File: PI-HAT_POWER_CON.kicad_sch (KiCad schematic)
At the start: 2 parts, among them J101 282834-2, J102 Raspberry_Pi_2x20_PTH_NoSilk

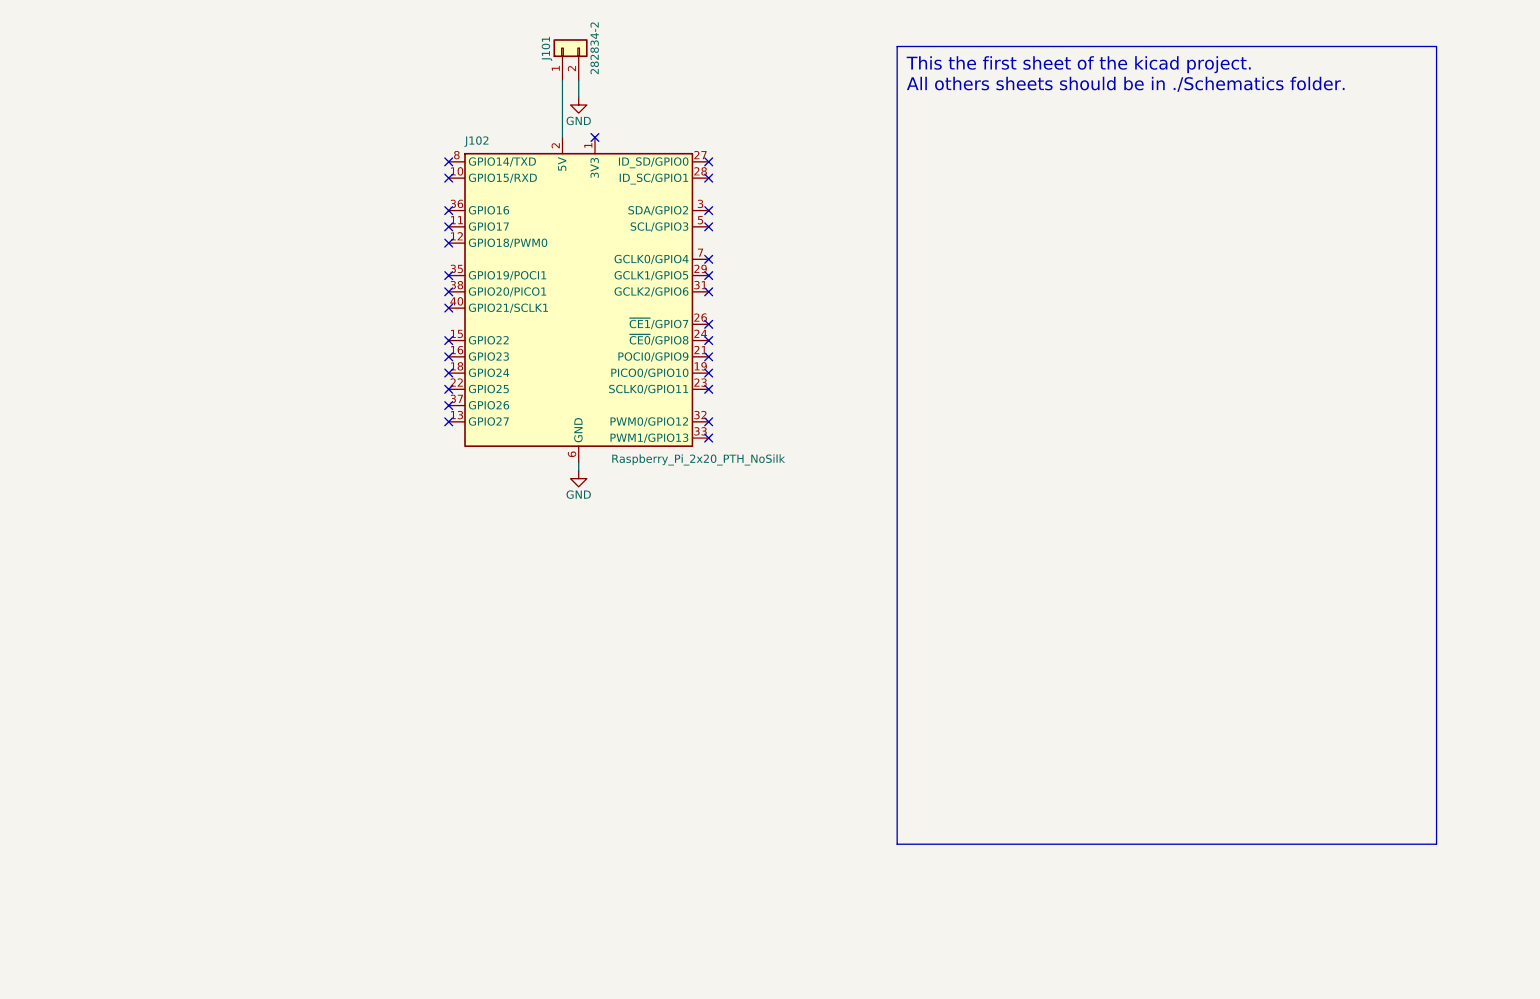
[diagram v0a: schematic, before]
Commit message: Add M41T0M6 RTC component to project schematic, PCB, and project settings
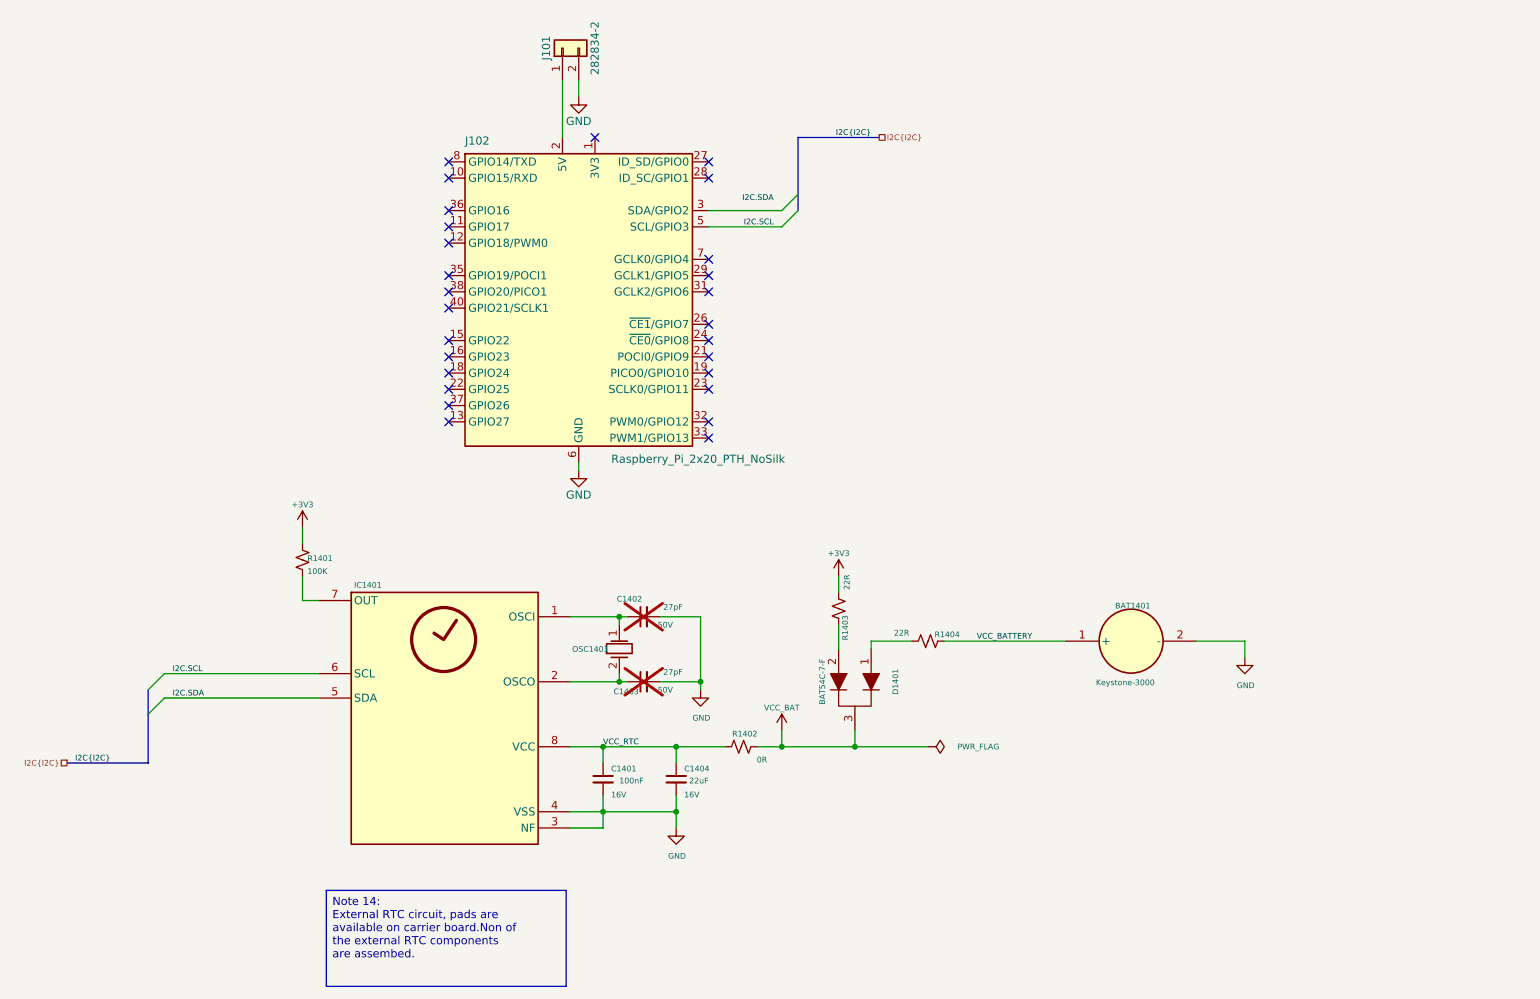
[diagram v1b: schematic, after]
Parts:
- added BAT1401: Keystone-3000, 0_NORTEK_DIVERS_LOCAL:T_Keystone_3000, symbol 0_NORTEK_NORTEKGLOBAL:Keystone-3000
- added C1401: 100nF, Capacitor_SMD:C_0603_1608Metric, symbol Device:C_Small
- added C1402, C1403: 27pF, Capacitor_SMD:C_0603_1608Metric, symbol Device:C_Small
- added C1404: 22uF, Capacitor_SMD:C_1210_3225Metric, symbol Device:C_Small
- added D1401: BAT54C-7-F, Package_TO_SOT_SMD:SOT-23-3, symbol 0_NORTEK_NORTEKDIODE:BAT54C-7-F
- added IC1401: M41T0M6, Package_SO:SOIC-8_3.9x4.9mm_P1.27mm, symbol 0_NORTEK_NORTEKGLOBAL:M41T0M6
- added OSC1401: CC4V-T1A, 0_NORTEK_GLOBAL:T_MC_CC4V-T1A, symbol 0_NORTEK_NORTEKGLOBAL:CC4V-T1A-32.768KHz-30ppm-5x1.9mm
- added R1401: 100K, Resistor_SMD:R_0603_1608Metric, symbol Device:R_Small_US
- added R1402: 0R, Resistor_SMD:R_0603_1608Metric, symbol Device:R_Small_US
- added R1403, R1404: 22R, Resistor_SMD:R_0603_1608Metric, symbol Device:R_Small_US
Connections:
- net GND: now also BAT1401.2 (-), C1401.2, C1402.2, C1403.2, C1404.2, IC1401.3 (NF), IC1401.4 (VSS)
- net I2C.SCL: now reaches J102.5 (SCL/GPIO3)
- net I2C.SCL: now also IC1401.6 (SCL)
- new net: C1402.1, IC1401.1 (OSCI), OSC1401.1 (OSC1)
- new net: D1401.2, R1403.1
- new net: D1401.1, R1404.2
- new net: C1403.1, IC1401.2 (OSCO), OSC1401.2 (OSC2)
- new net: IC1401.7 (OUT), R1401.2
- new net +3V3: R1401.1, R1403.2
- new net I2C.SDA: IC1401.5 (SDA)
- new net VCC_BAT: D1401.3, R1402.2
- new net VCC_BATTERY: BAT1401.1 (+), R1404.1
- new net VCC_RTC: C1401.1, C1404.1, IC1401.8 (VCC), R1402.1
- no-connect marks 29 -> 27

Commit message: Route PCB: Complete all nets, DRC clear, power and RTC connectivity verified
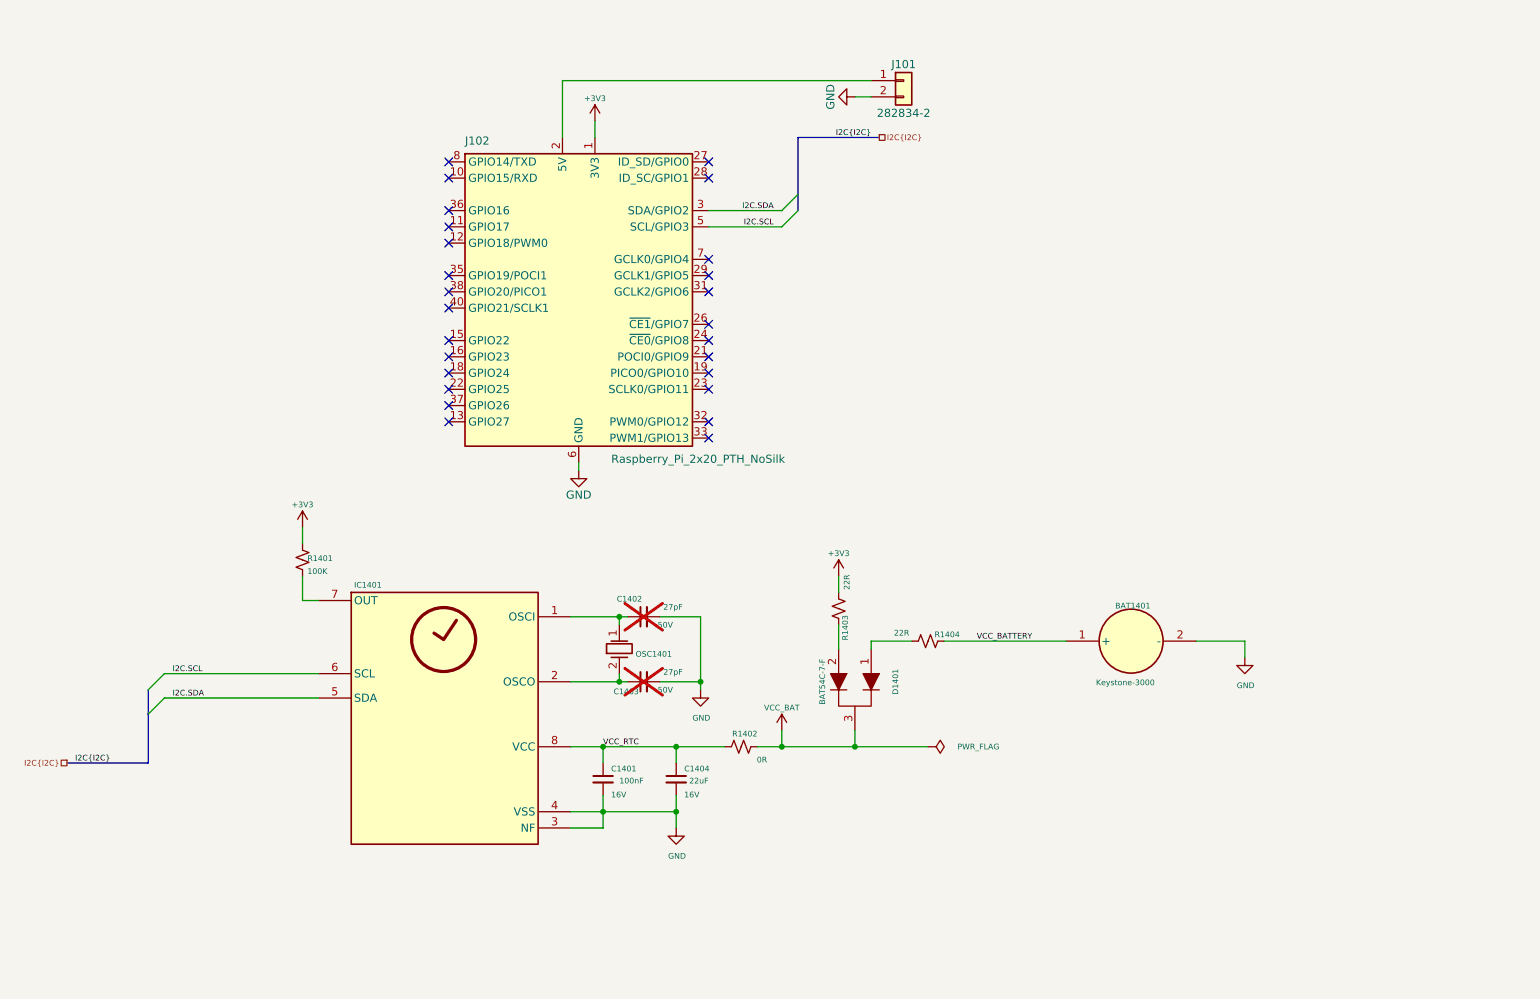
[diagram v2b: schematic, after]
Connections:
- net +3V3: now also J102.1 (3V3), J102.17 (3V3)
- net I2C.SDA: now also J102.3 (SDA/GPIO2)
- no-connect marks 27 -> 26
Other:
- moved on the sheet: J101
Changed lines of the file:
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@@
 		(company "NortekMed")
 	)
-	(text_box "Note 14:\n  External RTC circuit, pads are           available on carrier board.Non of       the external RTC components           are assembed."
-		(exclude_from_sim no)
-		(at 123.77 157.08 0)
-		(size -37.5 15)
-		(margins 0.9525 0.9525 0.9525 0.9525)
-		(stroke
-			(width 0)
-			(type default)
-			(color 0 0 0 1)
-		)
-		(fill
-			(type color)
-			(color 207 201 181 1)
-		)
-		(effects
-			(font
-				(size 1.27 1.27)
-			)
-			(justify left top)
-		)
-	)
 	(junction
 		(at 168.91 134.62)
@@
 	)
 	(no_connect
-		(at 128.27 39.37)
-	)
-	(no_connect
 		(at 105.41 50.8)
 	)
@@
 	(wire
 		(pts
+			(xy 128.27 36.83) (xy 128.27 39.37)
+		)
+		(stroke
+			(width 0)
+			(type default)
+		)
+	)
+	(wire
+		(pts
 			(xy 124.46 147.32) (xy 129.54 147.32)
 		)
@@
 	(wire
 		(pts
+			(xy 123.19 30.48) (xy 171.45 30.48)
+		)
+		(stroke
+			(width 0)
+			(type default)
+		)
+	)
+	(wire
+		(pts
 			(xy 124.46 124.46) (xy 132.08 124.46)
 		)
@@
 	(wire
 		(pts
-			(xy 125.73 33.02) (xy 125.73 30.48)
+			(xy 168.91 33.02) (xy 171.45 33.02)
 		)
 		(stroke
@@
 	)
 	(label "I2C.SDA"
-		(at 156.21 49.53 180)
+		(at 156.21 50.8 180)
 		(effects
 			(font
@@
 	(symbol
 		(lib_id "0_NORTEK_NORTEKCON:282834-2")
-		(at 123.19 25.4 90)
+		(at 176.53 30.48 0)
 		(unit 1)
 		(body_style 1)
@@
 		(dnp no)
 		(property "Reference" "J101"
-			(at 120.65 25.4 0)
+			(at 176.53 27.94 0)
 			(show_name no)
 			(do_not_autoplace no)
@@
 		)
 		(property "Value" "282834-2"
-			(at 128.27 25.4 0)
+			(at 176.53 35.56 0)
 			(show_name no)
 			(do_not_autoplace no)
@@
 		)
 		(property "Footprint" "0_NORTEK_CONNECTOR_LOCAL:TE_282834-2"
-			(at 130.81 22.225 0)
+			(at 179.705 38.1 0)
 			(hide yes)
 			(show_name no)
@@
 		)
 		(property "Datasheet" "https://www.farnell.com/datasheets/3651102.pdf"
-			(at 132.715 24.13 0)
+			(at 177.8 40.005 0)
 			(hide yes)
 			(show_name no)
@@
 		)
 		(property "Description" "Bornier fil-à-carte, 2.54 mm, 2 Voies, 30 AWG, 16 AWG, 1.4 mm², Par vis"
-			(at 123.19 25.4 0)
+			(at 176.53 30.48 0)
 			(hide yes)
 			(show_name no)
@@
 		)
 		(property "mfr" "BUCHANAN - TE CONNECTIVITY"
-			(at 134.62 24.765 0)
+			(at 177.165 41.91 0)
 			(hide yes)
 			(show_name no)
@@
 		)
 		(property "mfr #" "282834-2"
-			(at 134.62 3.175 0)
+			(at 198.755 41.91 0)
 			(hide yes)
 			(show_name no)
@@
 		)
 		(property "vendor1" "FARNELL"
-			(at 139.065 25.4 0)
+			(at 176.53 46.355 0)
 			(hide yes)
 			(show_name no)
@@
 		)
 		(property "vendor1 #" "2112482"
-			(at 139.065 15.875 0)
+			(at 186.055 46.355 0)
 			(hide yes)
 			(show_name no)
@@
 		)
 		(property "TOLERANCE" ""
-			(at 123.19 25.4 0)
+			(at 176.53 30.48 0)
 			(hide yes)
 			(show_name no)
@@
 		)
 		(property "TYPE" ""
-			(at 123.19 25.4 0)
+			(at 176.53 30.48 0)
 			(hide yes)
 			(show_name no)
@@
 		)
 		(property "RATING" ""
-			(at 123.19 25.4 0)
+			(at 176.53 30.48 0)
 			(hide yes)
 			(show_name no)
@@
 		)
 		(property "vendor2" ""
-			(at 123.19 25.4 0)
+			(at 176.53 30.48 0)
 			(hide yes)
 			(show_name no)
@@
 		)
 		(property "vendor2 #" ""
-			(at 123.19 25.4 0)
+			(at 176.53 30.48 0)
 			(hide yes)
 			(show_name no)
@@
 		(dnp no)
 		(property "Reference" "OSC1401"
-			(at 124.714 119.888 0)
+			(at 134.62 120.65 0)
 			(show_name no)
 			(do_not_autoplace no)
@@
 	)
 	(symbol
+		(lib_id "power:+3V3")
+		(at 128.27 36.83 0)
+		(unit 1)
+		(body_style 1)
+		(exclude_from_sim no)
+		(in_bom yes)
+		(on_board yes)
+		(in_pos_files yes)
+		(dnp no)
+		(property "Reference" "#PWR0103"
+			(at 128.27 40.64 0)
+			(hide yes)
+			(show_name no)
+			(do_not_autoplace no)
+			(effects
+				(font
+					(size 0.889 0.889)
+				)
+			)
+		)
+		(property "Value" "+3V3"
+			(at 128.27 33.274 0)
+			(show_name no)
+			(do_not_autoplace no)
+			(effects
+				(font
+					(size 0.889 0.889)
+				)
+			)
+		)
+		(property "Footprint" ""
+			(at 128.27 36.83 0)
+			(hide yes)
+			(show_name no)
+			(do_not_autoplace no)
+			(effects
+				(font
+					(size 0.889 0.889)
+				)
+			)
+		)
+		(property "Datasheet" ""
+			(at 128.27 36.83 0)
+			(hide yes)
+			(show_name no)
+			(do_not_autoplace no)
+			(effects
+				(font
+					(size 0.889 0.889)
+				)
+			)
+		)
+		(property "Description" "Power symbol creates a global label with name \"+3V3\""
+			(at 128.27 36.83 0)
+			(hide yes)
+			(show_name no)
+			(do_not_autoplace no)
+			(effects
+				(font
+					(size 0.889 0.889)
+				)
+			)
+		)
+		(pin "1"
+		)
+		(instances
+			(project "PI-HAT_POWER_CON"
+				(path "/ed9ec358-b12f-4bde-8de4-e801f410db11"
+					(reference "#PWR0103")
+					(unit 1)
+				)
+			)
+		)
+	)
+	(symbol
 		(lib_id "power:GND")
-		(at 125.73 33.02 0)
+		(at 168.91 33.02 270)
 		(unit 1)
 		(body_style 1)
@@
 		(dnp no)
 		(property "Reference" "#PWR0102"
-			(at 125.73 39.37 0)
+			(at 162.56 33.02 0)
 			(hide yes)
 			(show_name no)
@@
 		)
 		(property "Value" "GND"
-			(at 125.73 36.83 0)
+			(at 165.1 33.02 0)
 			(show_name no)
 			(do_not_autoplace no)
@@
 		)
 		(property "Footprint" ""
-			(at 125.73 33.02 0)
+			(at 168.91 33.02 0)
 			(hide yes)
 			(show_name no)
@@
 		)
 		(property "Datasheet" ""
-			(at 125.73 33.02 0)
+			(at 168.91 33.02 0)
 			(hide yes)
 			(show_name no)
@@
 		)
 		(property "Description" "Power symbol creates a global label with name \"GND\" , ground"
-			(at 125.73 33.02 0)
+			(at 168.91 33.02 0)
 			(hide yes)
 			(show_name no)

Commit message: prepare for v300326 production
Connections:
- net +5.1V: now reaches J101.1 (Pin_1), J102.2 (5V), J102.4 (5V)
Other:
- title: PROJECT_NAME -> PI_RTC_POWER
